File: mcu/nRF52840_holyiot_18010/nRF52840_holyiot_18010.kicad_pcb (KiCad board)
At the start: 2 copper layers, 3 parts

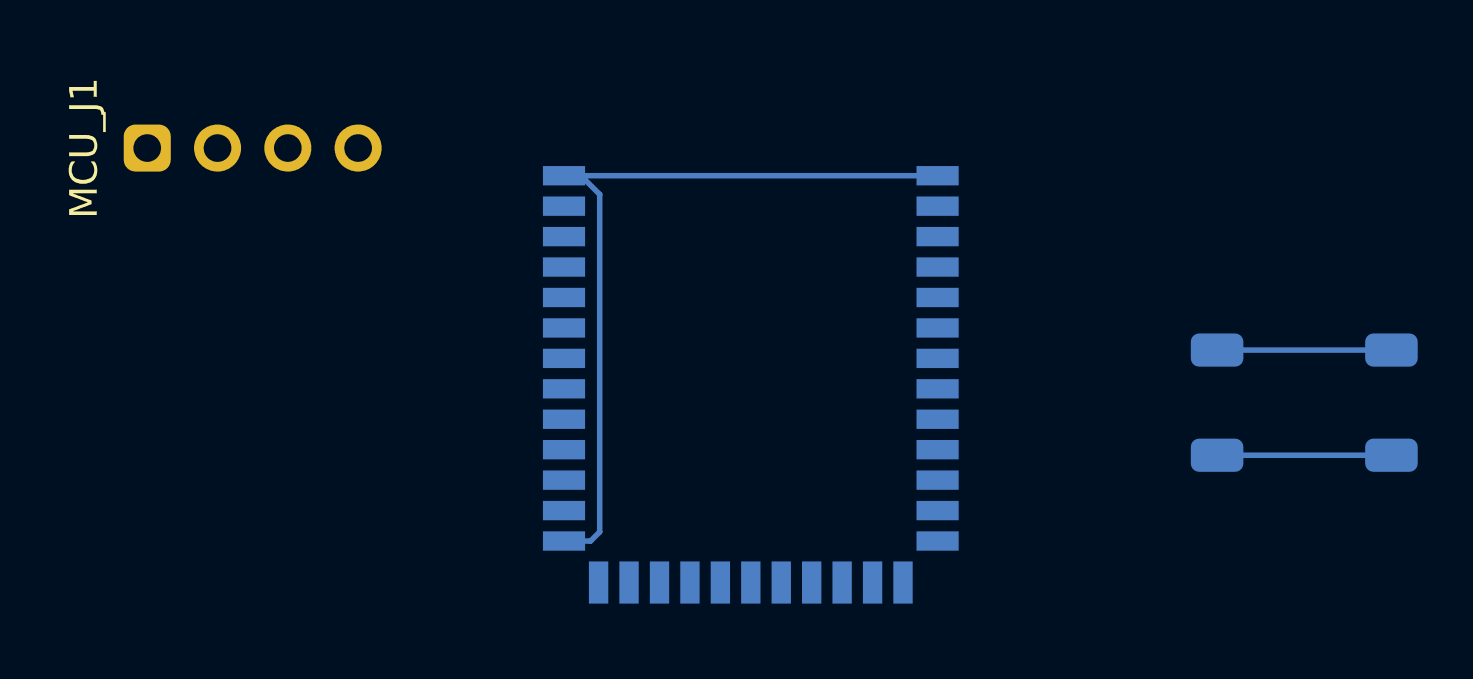
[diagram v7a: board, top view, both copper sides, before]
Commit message: add gnd via in mcu
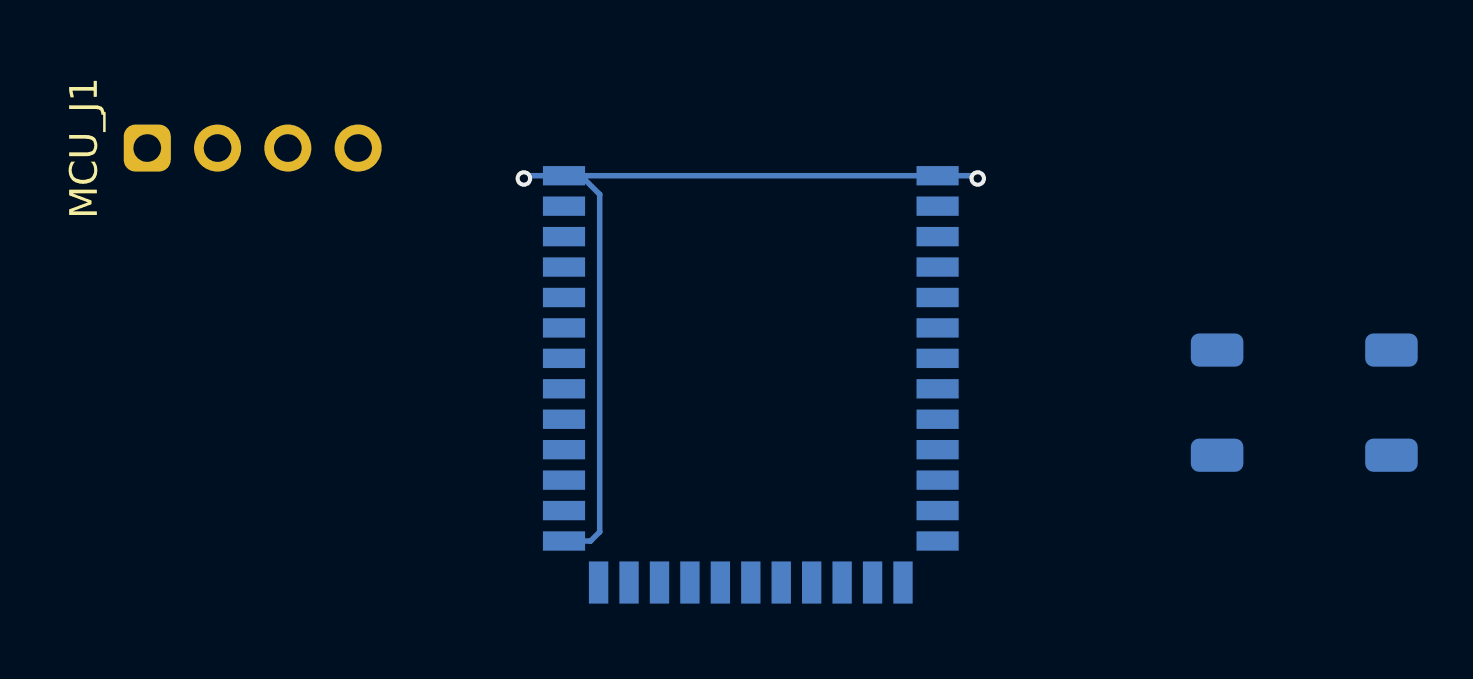
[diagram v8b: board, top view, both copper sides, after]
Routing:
- net RESET: track 6.30 -> 0.00 mm
- net GND: track 35.0 -> 31.7 mm, vias 0 -> 2
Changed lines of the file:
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@@
 		)
 	)
+	(via
+		(at -8.2 -5.6)
+		(size 0.6)
+		(drill 0.3)
+		(layers "F.Cu" "B.Cu")
+		(net 3)
+	)
+	(via
+		(at 8.2 -5.6)
+		(size 0.6)
+		(drill 0.3)
+		(layers "F.Cu" "B.Cu")
+		(net 3)
+	)
 	(segment
-		(start 16.85 0.6)
-		(end 23.15 0.6)
+		(start -6.75 -5.7)
+		(end -8.1 -5.7)
+		(width 0.2)
+		(layer "B.Cu")
+		(net 3)
+	)
+	(segment
+		(start 6.75 -5.7)
+		(end 8.1 -5.7)
+		(width 0.2)
+		(layer "B.Cu")
+		(net 3)
+	)
+	(segment
+		(start 8.1 -5.7)
+		(end 8.2 -5.6)
 		(width 0.2)
 		(layer "B.Cu")
@@
 	)
 	(segment
+		(start -8.1 -5.7)
+		(end -8.2 -5.6)
+		(width 0.2)
+		(layer "B.Cu")
+		(net 3)
+	)
+	(segment
 		(start -5.788 7.5)
 		(end -5.46 7.172)
@@
 		(net 3)
 	)
-	(segment
-		(start 16.85 4.4)
-		(end 23.15 4.4)
-		(width 0.2)
-		(layer "B.Cu")
-		(net 5)
-	)
 	(embedded_fonts no)
